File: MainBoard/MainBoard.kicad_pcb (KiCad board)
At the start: 2 copper layers, 120 x 151 mm, 63 parts, among them J1 Conn_02x19_Odd_Even, J2 SER1, J3 Conn_02x19_Odd_Even, J4 SER2, J5 Conn_01x04_Pin, J6 JST, J7 Conn_01x02_Socket, J8 UART, J9 Conn_01x05_Socket, Q1 MMBT3904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

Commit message: routing
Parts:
- J6: footprint Connector_JST:JST_PH_S2B-PH-K_1x02_P2.00mm_Horizontal -> Connector_JST:JST_PH_B2B-PH-K_1x02_P2.00mm_Vertical
- moved R3 131.9 mm to (51.0, 47.0)
- moved R4 128.9 mm to (54.0, 47.0)
- moved J6 57.5 mm to (76.0, 104.0), turned to 90 degrees
- moved J8 53.5 mm to (131.0, 75.4)
- moved C1 46.7 mm to (84.0, 120.0), turned to -90 degrees
- moved R14 39.1 mm to (77.0, 121.0), turned to 90 degrees
- moved R13 39.0 mm to (74.0, 121.0), turned to -90 degrees
- moved U2 22.8 mm to (47.0, 46.0), turned to 90 degrees
- moved C4 18.4 mm to (52.5, 42.8)
- moved JP1 15.3 mm to (76.0, 89.9), turned to 0 degrees
- moved C3 15.0 mm to (98.5, 124.0), turned to 90 degrees
- moved R6 14.0 mm to (92.0, 119.0), turned to 180 degrees
- moved C6 12.0 mm to (109.0, 123.0)
- moved C7 12.0 mm to (113.0, 123.0)
- moved L1 12.0 mm to (104.0, 122.0)
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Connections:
- J1 pad 6: +3V3 -> unconnected-(J1-Pin_6-Pad6)
- J5 pad 3: /ENC2A -> /M2A
- J5 pad 4: /ENC2B -> /M2B
- Q2 pad 2: /SENS3 -> /SENS1
- Q3 pad 2: /SENS1 -> /SENS2
- Q4 pad 2: /SENS4 -> /SENS3
- Q5 pad 2: /SENS2 -> /SENS4
- R10 pad 1: /SENS3 -> /SENS1
- R15 pad 1: /SENS1 -> /SENS2
- R16 pad 1: /SENS4 -> /SENS3
- R19 pad 1: /SENS2 -> /SENS4
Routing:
- net +3V3: track 0.00 -> 300.7 mm, vias 0 -> 2
- net +5V: track 0.00 -> 204.6 mm, vias 0 -> 1
- net +BATT: track 0.00 -> 198.6 mm, vias 0 -> 1
- net /MAG_TRIG: track 0.00 -> 179.2 mm, vias 0 -> 1
- net /SDA: track 0.00 -> 178.8 mm, vias 0 -> 1
- net /SCL: track 0.00 -> 176.9 mm, vias 0 -> 2
- net /VLED: track 0.00 -> 124.1 mm
- net /RX: track 0.00 -> 122.7 mm, vias 0 -> 1
- net /TX: track 0.00 -> 120.3 mm, vias 0 -> 1
- net /SENS0: track 0.00 -> 114.6 mm
- net /SER1: track 0.00 -> 106.5 mm, vias 0 -> 1
- net /SENS5: track 0.00 -> 102.9 mm
- net /SENS1: track 0.00 -> 101.4 mm
- net /SENS2: track 0.00 -> 98.2 mm
- net /SENS4: track 0.00 -> 91.2 mm
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- added copper zone on B.Cu, net GND
- added copper zone on F.Cu, net GND
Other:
- board text added: "EXT"
- board text added: "GND"
- board text added: "NUC"
- board text removed: "NUC EXT"

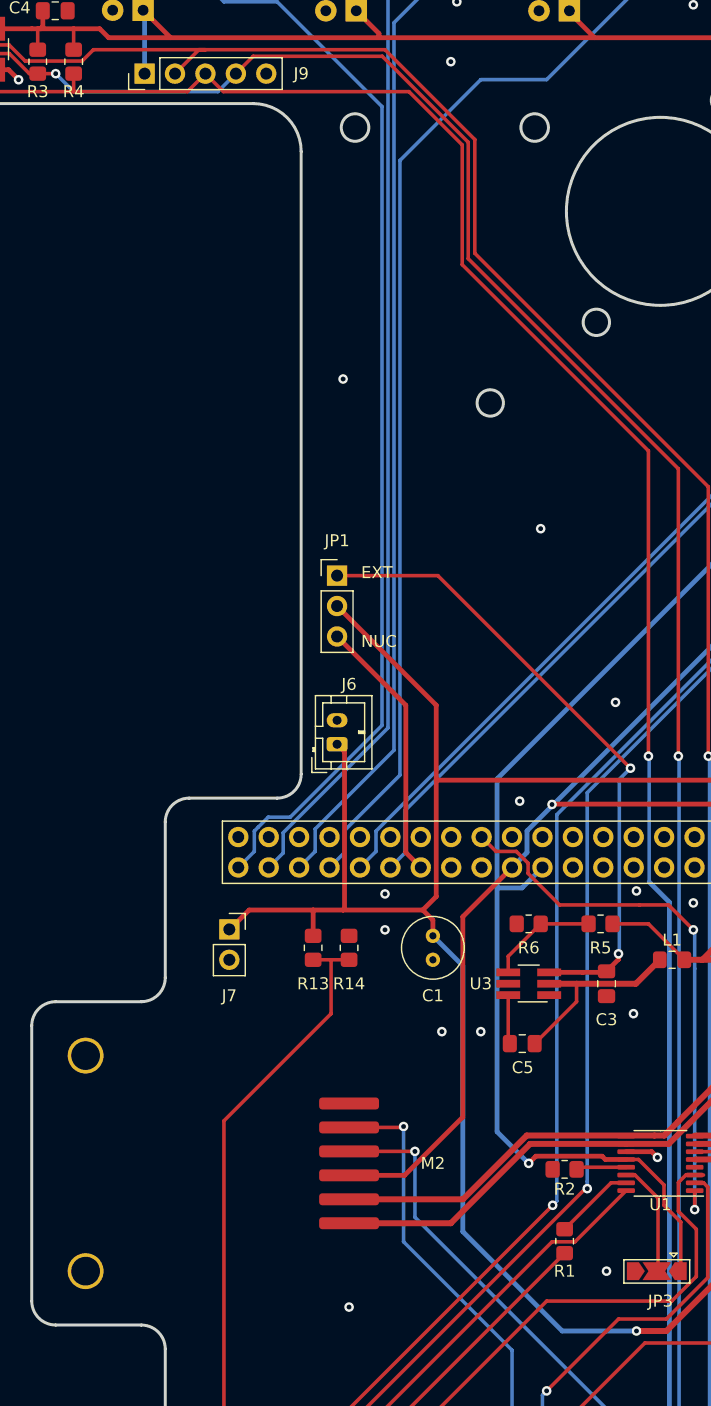
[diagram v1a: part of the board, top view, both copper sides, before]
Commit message: add logo
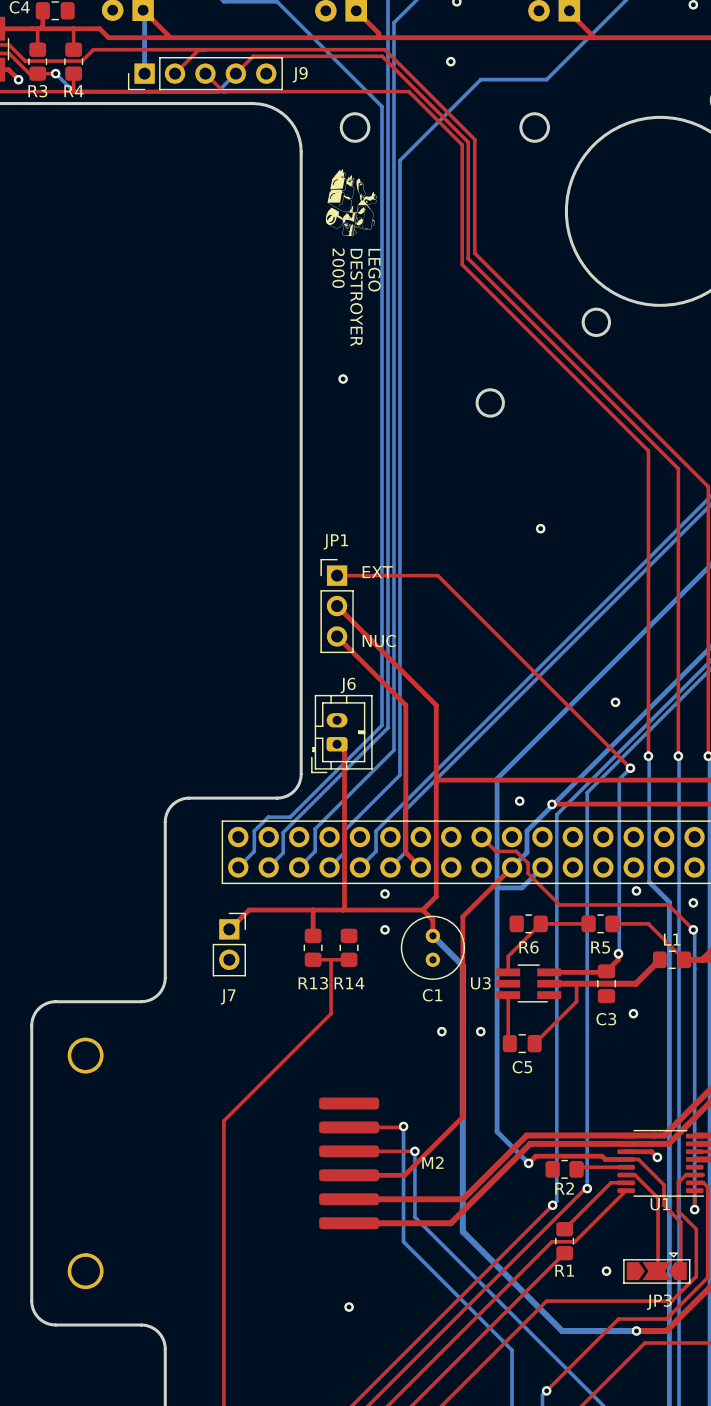
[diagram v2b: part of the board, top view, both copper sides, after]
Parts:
- added REF**: Logo, MainBoard:Logo, F.Cu at (82.0, 59.0)
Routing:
- net /SDA: track 178.8 -> 179.9 mm

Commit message: update routing
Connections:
- J3 pad 31: unconnected-(J3-Pin_31-Pad31) -> GND
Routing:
- net +3V3: track 300.7 -> 361.4 mm, vias 2 -> 3
- net /SENS0: track 114.6 -> 136.6 mm
- net /SENS1: track 101.4 -> 115.6 mm
- net Net-(U3-FB): track 9.17 -> 11.0 mm
- net /SENS2: track 98.2 -> 99.1 mm
- net GND: vias 35 -> 42

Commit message: update routing
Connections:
- J1 pad 15: unconnected-(J1-Pin_15-Pad15) -> +3V3
- J1 pad 17: +3V3 -> +5V
- J1 pad 19: +5V -> GND
- J1 pad 23: GND -> /VIN_NUC
- J1 pad 25: /VIN_NUC -> unconnected-(J1-Pin_25-Pad25)
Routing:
- net /SENS_BATT: track 65.0 -> 61.1 mm, vias 0 -> 1
- net +3V3: track 361.4 -> 364.0 mm
- net Net-(JP1-A): track 53.9 -> 56.3 mm
- net +5V: track 204.6 -> 205.8 mm
- net /VIN_NUC: track 22.2 -> 23.2 mm
- net /EN1: track 46.4 -> 47.0 mm
- net GND: vias 42 -> 43
